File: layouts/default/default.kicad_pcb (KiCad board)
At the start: 2 copper layers, 46 parts

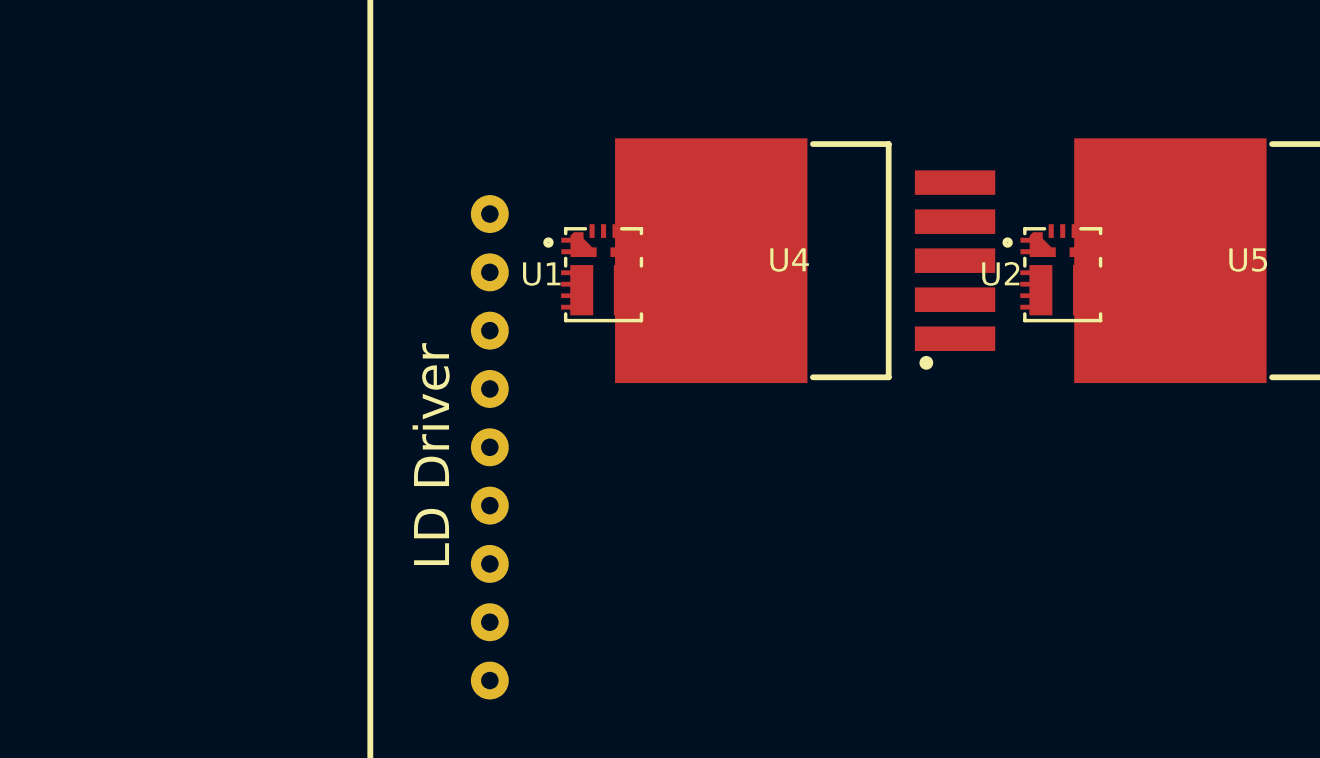
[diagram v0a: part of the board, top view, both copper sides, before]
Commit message: more connectors
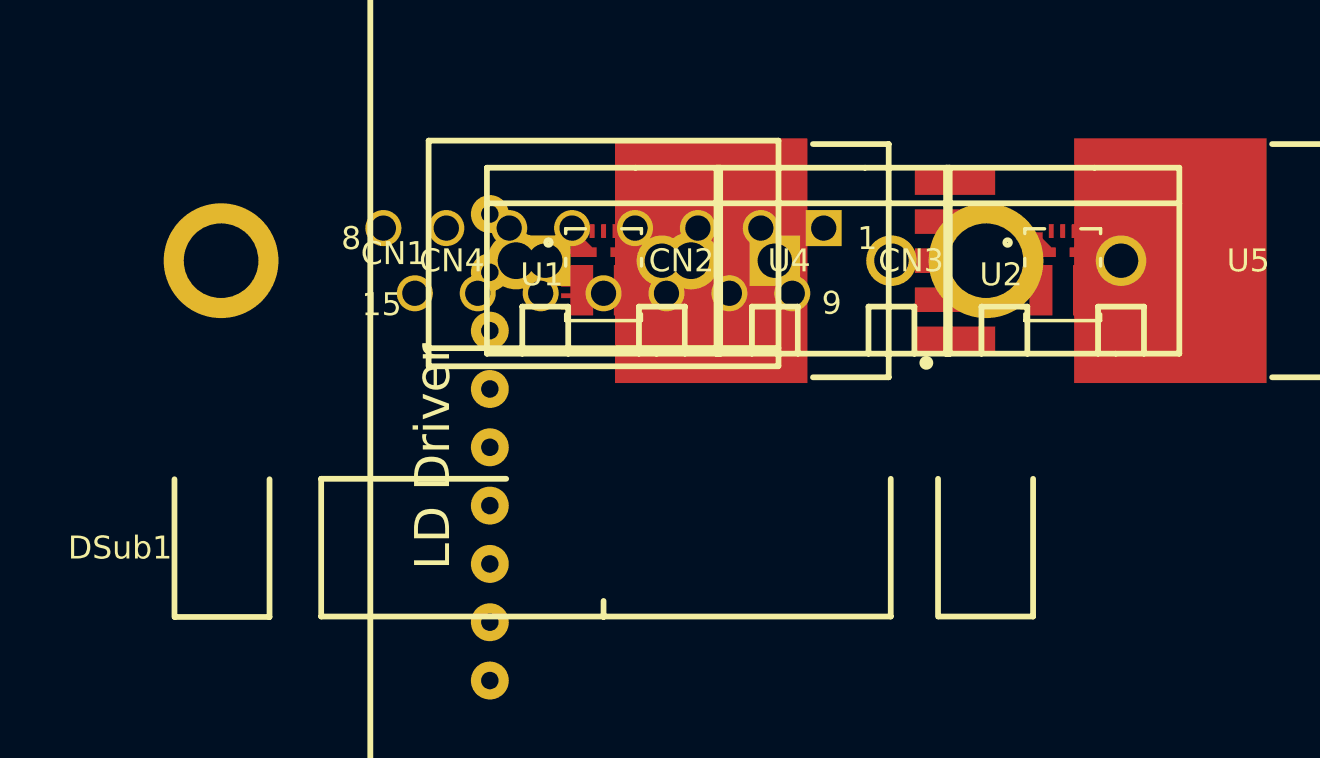
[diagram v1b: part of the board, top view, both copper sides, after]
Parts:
- added CN1: , Phoenix_Contact_1717729:CONN-TH_2P-P7.62_1717729, F.Cu at (0.00, 0.00)
- added CN2: , Phoenix_Contact_1729128:CONN-TH_2P-P5.08_1729128, F.Cu at (10.0, 0.00)
- added CN3: , Phoenix_Contact_1729128:CONN-TH_2P-P5.08_1729128, F.Cu at (20.0, 0.00)
- added CN4: , Phoenix_Contact_1729128:CONN-TH_2P-P5.08_1729128, F.Cu at (0.00, 0.00)
- added DSub1: , Omron_Electronics_XM3B_1522_502:DSUB-TH_15P-P2.74-S2.84_L18.5-W39.1-M, F.Cu at (0.00, 0.00)

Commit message: changing signals a bit
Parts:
- added C22: 100nF, YAGEO_CC0603KRX7R9BB104:C0603, F.Cu at (150.0, -230.0)
- added J2: , RFENABLE:RFENABLE, F.Cu at (134.5, 71.0)
- added J3: , VTUNE:VTUNE, F.Cu at (134.5, 41.0)
- added L1: L 100µH, TDK_NLV32T_101J_PF:L1210, F.Cu at (150.0, -40.0)
- added RF1: , BAT_WIRELESS_BWSMA_KE_Z001:SMA-TH_BWSMA-KE-Z001, F.Cu at (140.0, 0.00)
- C13, C16, C19: value 10µF -> 100nF; footprint Murata_Electronics_GRM21BZ71E106KE15L:C0805 -> YAGEO_CC0603KRX7R9BB104:C0603
- C14, C17, C20: value 100nF -> 10µF; footprint YAGEO_CC0603KRX7R9BB104:C0603 -> Murata_Electronics_GRM21BZ71E106KE15L:C0805
- CN1: footprint Phoenix_Contact_1717729:CONN-TH_2P-P7.62_1717729 -> Phoenix_Contact_1729128:CONN-TH_2P-P5.08_1729128
- CN2: footprint Phoenix_Contact_1729128:CONN-TH_2P-P5.08_1729128 -> Phoenix_Contact_1717729:CONN-TH_2P-P7.62_1717729
- moved C15 332.4 mm to (150.0, 0.00)
- moved C20 303.6 mm to (150.0, -390.0)
- moved R2 284.6 mm to (150.0, -10.0)
- moved R18 275.1 mm to (150.0, -30.0)
- moved R5 275.1 mm to (150.0, -80.0)
- moved R1 265.7 mm to (150.0, -60.0)
- moved R3 265.7 mm to (150.0, -130.0)
- moved R4 265.7 mm to (150.0, -120.0)
- moved J1 228.0 mm to (225.0, 37.0)
- moved R10 174.9 mm to (150.0, -270.0)
- moved R11 174.9 mm to (150.0, -220.0)
- moved R12 174.9 mm to (150.0, -330.0)
- moved R13 174.9 mm to (150.0, -320.0)
- moved R14 174.9 mm to (150.0, -280.0)
- moved R15 174.9 mm to (150.0, -380.0)
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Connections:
- C1 pad 1: input_caps[0]-power-hv -> hv
- C1 pad 2: input_caps[0]-power-lv -> lv
- C10 pad 1: input_caps[1]-power-hv-2 -> input_caps[0]-power-hv-2
- C10 pad 2: input_caps[1]-power-lv-2 -> input_caps[0]-power-lv-2
- C11 pad 1: output_caps[0]-power-hv-2 -> input_caps[1]-power-hv-2
- C11 pad 2: output_caps[0]-power-lv-2 -> input_caps[1]-power-lv-2
- C12 pad 1: output_caps[1]-power-hv-2 -> output_caps[0]-power-hv-2
- C12 pad 2: output_caps[1]-power-lv-2 -> output_caps[0]-power-lv-2
- C13 pad 1: ldo_7v-power_in-hv -> output_caps[1]-power-hv-2
- C13 pad 2: lv -> output_caps[1]-power-lv-2
- C14 pad 1: output_caps[0]-power-hv-3 -> ldo_7v-power_in-hv
- C14 pad 2: output_caps[0]-power-lv-3 -> reference-lv
- C15 pad 1: output_caps[1]-power-hv-3 -> output_caps[0]-power-hv-3
- C15 pad 2: output_caps[1]-power-lv-3 -> output_caps[0]-power-lv-3
- C16 pad 1: ldo_redpitaya-power_in-hv -> output_caps[1]-power-hv-3
- C16 pad 2: lv -> output_caps[1]-power-lv-3
- C17 pad 1: output_caps[0]-power-hv-4 -> ldo_redpitaya-power_in-hv
- C17 pad 2: output_caps[0]-power-lv-4 -> reference-lv
- C18 pad 1: output_caps[1]-power-hv-4 -> output_caps[0]-power-hv-4
- C18 pad 2: output_caps[1]-power-lv-4 -> output_caps[0]-power-lv-4
- C19 pad 1: ldo_vco-power_in-hv -> output_caps[1]-power-hv-4
- C19 pad 2: lv -> output_caps[1]-power-lv-4
- C2 pad 1: input_caps[1]-power-hv -> input_caps[0]-power-hv
- C2 pad 2: input_caps[1]-power-lv -> input_caps[0]-power-lv
- C20 pad 1: output_caps[0]-power-hv-5 -> ldo_vco-power_in-hv
- C20 pad 2: output_caps[0]-power-lv-5 -> reference-lv
- C21 pad 1: output_caps[1]-power-hv-5 -> output_caps[0]-power-hv-5
- C21 pad 2: output_caps[1]-power-lv-5 -> output_caps[0]-power-lv-5
- C3 pad 1: output_caps[0]-power-hv -> input_caps[1]-power-hv
- C3 pad 2: output_caps[0]-power-lv -> input_caps[1]-power-lv
- C4 pad 1: output_caps[1]-power-hv -> output_caps[0]-power-hv
- C4 pad 2: output_caps[1]-power-lv -> output_caps[0]-power-lv
- C5 pad 1: input_caps[0]-power-hv-1 -> output_caps[1]-power-hv
- C5 pad 2: input_caps[0]-power-lv-1 -> output_caps[1]-power-lv
- C6 pad 1: input_caps[1]-power-hv-1 -> input_caps[0]-power-hv-1
- C6 pad 2: input_caps[1]-power-lv-1 -> input_caps[0]-power-lv-1
- C7 pad 1: output_caps[0]-power-hv-1 -> input_caps[1]-power-hv-1
- C7 pad 2: output_caps[0]-power-lv-1 -> input_caps[1]-power-lv-1
- C8 pad 1: output_caps[1]-power-hv-1 -> output_caps[0]-power-hv-1
- C8 pad 2: output_caps[1]-power-lv-1 -> output_caps[0]-power-lv-1
- C9 pad 1: input_caps[0]-power-hv-2 -> output_caps[1]-power-hv-1
- C9 pad 2: input_caps[0]-power-lv-2 -> output_caps[1]-power-lv-1
- CN1 pad 1: hv -> ldo_redpitaya-power_out-hv
- CN1 pad 2: lv -> reference-lv
- CN2 pad 1: dps5005_1 -> buck_vco-power_in-hv
- CN2 pad 2: lv -> reference-lv
- CN3 pad 1: dps5005_2 -> dps5005_1
- CN3 pad 2: lv -> reference-lv
- CN4 pad 1: ldo_redpitaya-power_out-hv -> dps5005_2
- CN4 pad 2: lv -> reference-lv
- DSub1 pad 0: lv -> reference-lv
- DSub1 pad 8: vtune -> lv
- J1 pad GND1: lv -> reference-lv
- J1 pad GND2: lv -> reference-lv
- J1 pad GND3: lv -> reference-lv
- J1 pad GND4: lv -> reference-lv
- J1 pad GND5: lv -> reference-lv
- J1 pad GND6: lv -> reference-lv
- J1 pad GND7: lv -> reference-lv
- R1 pad 1: hv -> buck_vco-power_in-hv
- R11 pad 2: lv -> reference-lv
- R14 pad 2: lv -> reference-lv
- R17 pad 2: lv -> reference-lv
- R2 pad 2: lv -> reference-lv
- R4 pad 1: hv -> buck_vco-power_in-hv
- R5 pad 2: lv -> reference-lv
- R7 pad 1: hv -> buck_vco-power_in-hv
- R8 pad 2: lv -> reference-lv
- U1 pad 1: hv -> buck_vco-power_in-hv
- U1 pad 4: lv -> reference-lv
- U2 pad 1: hv -> buck_vco-power_in-hv
- U2 pad 4: lv -> reference-lv
- U3 pad 1: hv -> buck_vco-power_in-hv
- U3 pad 4: lv -> reference-lv
- U4 pad 3: lv -> reference-lv
- U4 pad 6: lv -> reference-lv
- U5 pad 3: lv -> reference-lv
- U5 pad 6: lv -> reference-lv
- U6 pad 3: lv -> reference-lv
- U6 pad 6: lv -> reference-lv

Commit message: adding more filtering
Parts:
- added C23: 100nF, YAGEO_CC0603KRX7R9BB104:C0603, F.Cu at (150.0, -20.0)
- added C24: 100nF, YAGEO_CC0603KRX7R9BB104:C0603, F.Cu at (150.0, -160.0)
- added C25: 10µF, Murata_Electronics_GRM21BZ71E106KE15L:C0805, F.Cu at (150.0, -460.0)
- added C26: 100nF, YAGEO_CC0603KRX7R9BB104:C0603, F.Cu at (150.0, -110.0)
- added C27: 100nF, YAGEO_CC0603KRX7R9BB104:C0603, F.Cu at (150.0, -250.0)
- added C28: 10µF, Murata_Electronics_GRM21BZ71E106KE15L:C0805, F.Cu at (150.0, 0.00)
- added C29: 100nF, YAGEO_CC0603KRX7R9BB104:C0603, F.Cu at (150.0, -200.0)
- added C30: 100nF, YAGEO_CC0603KRX7R9BB104:C0603, F.Cu at (150.0, -330.0)
- added L2: L 10µH, XR_XRTC322512S100MBCA:IND-SMD_L3.2-W2.5_CKST322512-2.2UH, F.Cu at (150.0, -380.0)
- added L3: L 10µH, XR_XRTC322512S100MBCA:IND-SMD_L3.2-W2.5_CKST322512-2.2UH, F.Cu at (150.0, -60.0)
- C14, C20: footprint Murata_Electronics_GRM21BZ71E106KE15L:C0805 -> Samsung_Electro_Mechanics_CL21B106KOQNNNE:C0805
- C15, C19, C21: footprint YAGEO_CC0603KRX7R9BB104:C0603 -> Samsung_Electro_Mechanics_CL05B104KO5NNNC:C0402
- C16, C18: value 100nF -> 10µF; footprint YAGEO_CC0603KRX7R9BB104:C0603 -> Samsung_Electro_Mechanics_CL21B106KOQNNNE:C0805
- C17: value 10µF -> 100nF; footprint Murata_Electronics_GRM21BZ71E106KE15L:C0805 -> Samsung_Electro_Mechanics_CL05B104KO5NNNC:C0402
- C22: value 100nF -> 10µF; footprint YAGEO_CC0603KRX7R9BB104:C0603 -> Murata_Electronics_GRM21BZ71E106KE15L:C0805
- moved C16 390.0 mm to (150.0, -500.0)
- moved C2 390.0 mm to (150.0, -10.0)
- moved C18 280.0 mm to (150.0, -350.0)
- moved L1 240.0 mm to (150.0, -280.0)
- moved C1 220.0 mm to (150.0, -30.0)
- moved C22 170.0 mm to (150.0, -400.0)
- moved J1 169.1 mm to (60.0, 0.00)
- moved C14 160.0 mm to (150.0, -130.0)
- moved C20 160.0 mm to (150.0, -230.0)
- moved R15 160.0 mm to (150.0, -220.0)
- moved C19 140.0 mm to (150.0, -310.0)
- moved C17 120.0 mm to (150.0, -470.0)
- moved C9 120.0 mm to (150.0, -480.0)
- moved R16 120.0 mm to (150.0, -490.0)
- moved DSub1 112.0 mm to (110.0, 0.00)
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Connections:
- C14 pad 1: ldo_7v-power_in-hv -> ldo_redpitaya-power_out-hv
- C15 pad 1: output_caps[0]-power-hv-3 -> ldo_redpitaya-power_out-hv
- C15 pad 2: output_caps[0]-power-lv-3 -> reference-lv
- C16 pad 1: output_caps[1]-power-hv-3 -> filter_5v_rp-power_out-hv
- C16 pad 2: output_caps[1]-power-lv-3 -> reference-lv
- C17 pad 1: ldo_redpitaya-power_in-hv -> filter_5v_rp-power_out-hv
- C18 pad 1: output_caps[0]-power-hv-4 -> filter_15v-power_in-hv
- C18 pad 2: output_caps[0]-power-lv-4 -> reference-lv
- C19 pad 1: output_caps[1]-power-hv-4 -> filter_15v-power_in-hv
- C19 pad 2: output_caps[1]-power-lv-4 -> reference-lv
- C20 pad 1: ldo_vco-power_in-hv -> filter_15v-power_out-hv
- C21 pad 1: output_caps[0]-power-hv-5 -> filter_15v-power_out-hv
- C21 pad 2: output_caps[0]-power-lv-5 -> reference-lv
- C22 pad 1: output_caps[1]-power-hv-5 -> ldo_7v-power_in-hv
- C22 pad 2: output_caps[1]-power-lv-5 -> reference-lv
- CN1 pad 1: ldo_redpitaya-power_out-hv -> filter_5v_rp-power_out-hv
- CN2 pad 1: buck_vco-power_in-hv -> filter_15v-power_in-hv
- R1 pad 1: buck_vco-power_in-hv -> filter_15v-power_out-hv
- R4 pad 1: buck_vco-power_in-hv -> filter_15v-power_out-hv
- R7 pad 1: buck_vco-power_in-hv -> filter_15v-power_out-hv
- U1 pad 1: buck_vco-power_in-hv -> filter_15v-power_out-hv
- U2 pad 1: buck_vco-power_in-hv -> filter_15v-power_out-hv
- U3 pad 1: buck_vco-power_in-hv -> filter_15v-power_out-hv

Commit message: fixing dps5005 connections
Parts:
- C14, C16, C18, C20: footprint Samsung_Electro_Mechanics_CL21B106KOQNNNE:C0805 -> Murata_Electronics_GRM21BZ71E106KE15L:C0805
- C15, C17, C19, C21: footprint Samsung_Electro_Mechanics_CL05B104KO5NNNC:C0402 -> Samsung_Electro_Mechanics_CL05B104KB54PNC:C0402
- L1: value L 100µH -> L 470µH; footprint TDK_NLV32T_101J_PF:L1210 -> cjiang_FNR6045S471MT:IND-SMD_L6.0-W6.0_FNR60XXS
- L2, L3: footprint XR_XRTC322512S100MBCA:IND-SMD_L3.2-W2.5_CKST322512-2.2UH -> cjiang_FHD4020S_100MT:IND-SMD_L4.0-W4.0
- moved C22 390.0 mm to (150.0, -10.0)
- moved C5 390.0 mm to (150.0, -20.0)
- moved R14 390.0 mm to (150.0, 0.00)
- moved C12 380.0 mm to (150.0, -40.0)
- moved C9 380.0 mm to (150.0, -100.0)
- moved R12 380.0 mm to (150.0, -60.0)
- moved R13 380.0 mm to (150.0, -50.0)
- moved R17 380.0 mm to (150.0, -70.0)
- moved C25 370.0 mm to (150.0, -90.0)
- moved R16 370.0 mm to (150.0, -120.0)
- moved C18 320.0 mm to (150.0, -30.0)
- moved C21 240.0 mm to (150.0, -430.0)
- moved L1 180.0 mm to (150.0, -460.0)
- moved C16 160.0 mm to (150.0, -340.0)
- moved C10 150.0 mm to (150.0, -300.0)
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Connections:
- CN3 pad 1: dps5005_1 -> filter_15v-power_out-hv
- CN4 pad 1: dps5005_2 -> filter_15v-power_out-hv
